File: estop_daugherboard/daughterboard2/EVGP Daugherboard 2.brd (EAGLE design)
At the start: 82.6 x 94.6 mm, 39 parts, among them J1 E-STOP HEADER, J2 AVR_SPI_PROG_3X2PTH, J3 UX60-MB-5S8, U1 ATMEGA32U4-AU, U4 NL27WZ08USG, U5 N_FET1, U6 N_FET2, X1 TSX-3225 16.0000MF18X-AC0, X2 JST-XH-02-PIN-LONG-PAD, X3 JST-XH-02-PIN-LONG-PAD, X5 JST-XH-03-PIN-LONG-PAD, X6 JST-XH-03-PIN-LONG-PAD

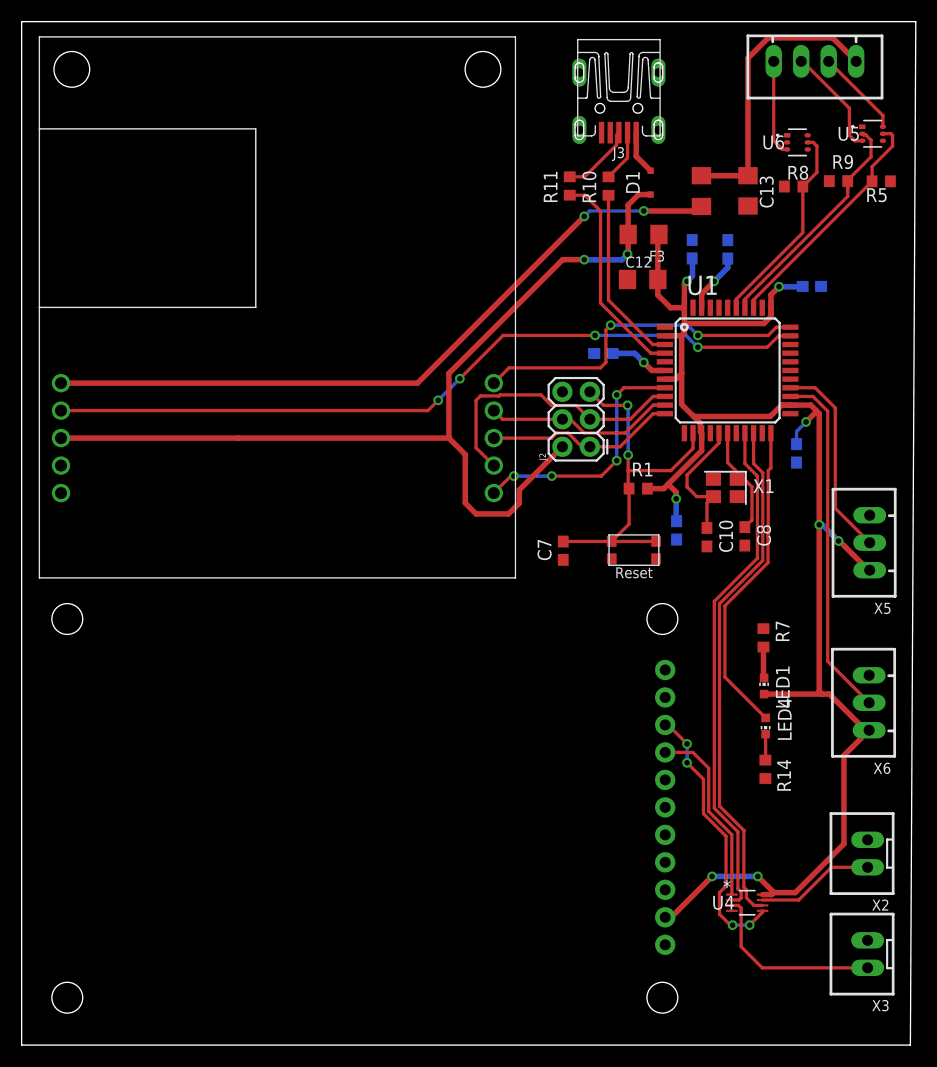
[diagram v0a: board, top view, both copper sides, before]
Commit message: Fixed up silkscreen
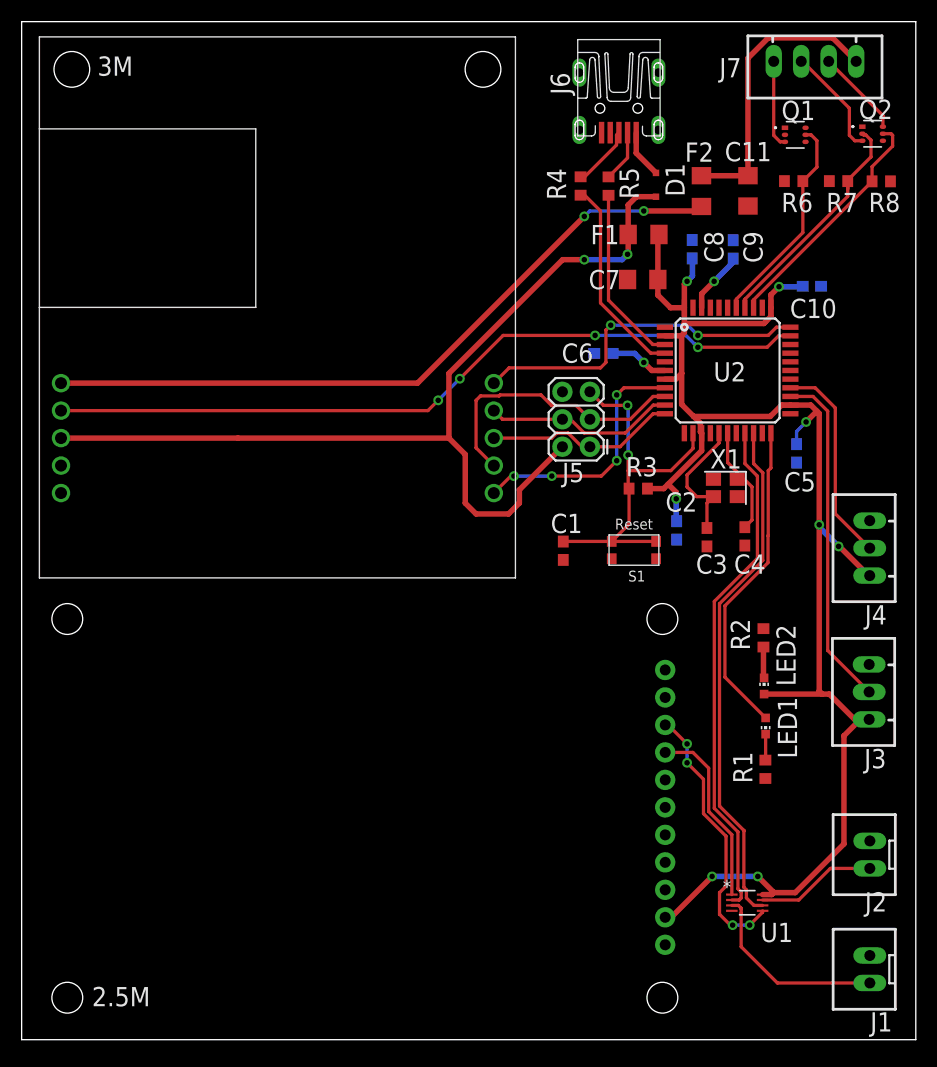
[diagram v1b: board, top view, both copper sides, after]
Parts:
- removed C12: 47uF, rcl:C1206
- removed LED4: BLUE, led:CHIP-LED0603
- removed R10, R11: 22 Ω, rcl:R0603
- removed R14: 330Ω, rcl:R0603
- removed R9: 10kΩ, rcl:R0603
- removed U4: NL27WZ08USG, DownloadedFiles:US8_2P40X2P10
- removed U6: N_FET2, DownloadedParts:SOT-363
- removed X2, X3: JST-XH-02-PIN-LONG-PAD, Rembrandt Electronics - JST XH Connectors v1-0:JST-XH-02-PACKAGE-LONG-PAD
- removed X5, X6: JST-XH-03-PIN-LONG-PAD, Rembrandt Electronics - JST XH Connectors v1-0:JST-XH-03-PACKAGE-LONG-PAD
- added C9: 10 nF, resistor:C0603
- added J4: JST-XH-03-PIN-LONG-PAD, Rembrandt Electronics - JST XH Connectors v1-0:JST-XH-03-PACKAGE-LONG-PAD
- added J5: AVR_SPI_PROG_3X2PTH, SparkFun-Connectors:2X3
- added J6: UX60-MB-5S8, RoboJackets-Connectors:UX60-MB-5S8
- added LED2: GREEN, led:CHIP-LED0603
- added Q1: N_FET2, DownloadedParts:SOT-363
- added R2: 330Ω, rcl:R0603
- added R3: 10k, rcl:R0603
- added R4: 22 Ω, rcl:R0603
- added R6: 10kΩ, rcl:R0603
- added RADIO: E-STOP HEADER, board_outline:RADIO_V1.3
- added U$1: (no value), RoboJackets-Aesthetics:ROBOBUZZ_1.0X
- added U2: ATMEGA32U4-AU, estop-v1.0:TQFP44
- C1: value 0.1 uF -> 0.1uF; device resistor:C0603 -> rcl:C0603
- C10, C8: value 9pF -> 0.1 uF
- C3: value 0.1 uF -> 9pF
- C4: value 1 uF -> 9pF
- C6: value 10 nF -> 1 uF
- C7: value 0.1uF -> 47uF; device rcl:C0603 -> rcl:C1206
- J1: value E-STOP HEADER -> JST-XH-02-PIN-LONG-PAD; device board_outline:RADIO_V1.3 -> Rembrandt Electronics - JST XH Connectors v1-0:JST-XH-02-PACKAGE-LONG-PAD
- J2: value AVR_SPI_PROG_3X2PTH -> JST-XH-02-PIN-LONG-PAD; device SparkFun-Connectors:2X3 -> Rembrandt Electronics - JST XH Connectors v1-0:JST-XH-02-PACKAGE-LONG-PAD
- J3: value UX60-MB-5S8 -> JST-XH-03-PIN-LONG-PAD; device RoboJackets-Connectors:UX60-MB-5S8 -> Rembrandt Electronics - JST XH Connectors v1-0:JST-XH-03-PACKAGE-LONG-PAD
- LED1: value GREEN -> BLUE
- R1: value 10k -> 330Ω
- R5: value 10kΩ -> 22 Ω
- R7: value 330Ω -> 10kΩ
- U1: value ATMEGA32U4-AU -> NL27WZ08USG; device estop-v1.0:TQFP44 -> DownloadedFiles:US8_2P40X2P10
- moved J1 84.2 mm to (84.4, 0.92), flipped to the top, turned to 90 degrees
- moved J3 64.6 mm to (84.3, 26.6), turned to 90 degrees
- moved U1 49.2 mm to (73.1, 7.07)
- moved J2 45.7 mm to (84.4, 11.5)
- moved R7 42.8 mm to (81.5, 73.8), turned to 0 degrees
- moved C1 30.3 mm to (56.1, 39.6), flipped to the top, turned to 270 degrees
- moved R1 28.5 mm to (74.7, 19.4), turned to 90 degrees
- moved C8 27.0 mm to (68.0, 67.5), flipped to the bottom, turned to 90 degrees
- moved C7 26.1 mm to (63.4, 64.7), turned to 0 degrees
- moved C2 25.8 mm to (66.5, 41.5), turned to 270 degrees
- moved R5 25.2 mm to (60.2, 73.3), turned to 90 degrees
- moved C10 25.1 mm to (79.0, 64.0), flipped to the bottom, turned to 180 degrees
- moved C4 21.4 mm to (72.8, 40.9), flipped to the top, turned to 270 degrees
- moved C6 15.0 mm to (59.8, 57.8), turned to 0 degrees
- moved R8 8.11 mm to (85.5, 73.7), turned to 180 degrees
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- renumbered C13 to C11, F3 to F1, F4 to F2, JST to J7, U5 to Q2
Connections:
- net 5V: now also C10.1, C7.2, C8.1, J3.1, J4.1, LED2.A, R3.2, RADIO.10, U1.8, U2.14, U2.2, U2.24, U2.34, U2.44, U2.7; no longer C1.1, C12.2, C3.1, J1.10, LED1.A, R1.2, U1.14, U1.2, U1.24, U1.34, U1.44, U1.7, U4.8, X5.1, X6.1
- net 5V_UNFUSED: now also J5.2; no longer J2.2
- net AREF: now also C9.1, U2.42; no longer C6.1, U1.42
- net DATA_N: now also R5.1, U2.3; no longer R10.1, U1.3
- net DATA_P: now also R4.1, U2.4; no longer R11.1, U1.4
- net DRIVE_EN: now also J2.1, U1.7; no longer U4.7, X2.1
- net DRIVE_EN_DB: now also U1.6, U2.20; no longer U1.20, U4.6
- net DRIVE_EN_RB: now also RADIO.3, U1.5; no longer J1.3, U4.5
- net ETH_RST: now also U2.32; no longer U1.32
- net GND: now also C7.1, C9.2, J1.2, J2.2, J3.3, J4.3, J5.6, J6.5, Q1.4, R1.1, R2.1, R6.1, RADIO.1, RADIO.11, U1.4, U2.15, U2.23, U2.35, U2.43, U2.5; no longer C12.1, C7.2, J1.1, J1.11, J2.6, J3.5, R14.1, R5.1, R9.1, U1.15, U1.23, U1.35, U1.43, U1.5, U4.4, U6.4, X2.2, X3.2, X5.3, X6.3
- net INTERRUPT: now also U2.33; no longer U1.33
- net LED1: now also LED1.A, U2.22; no longer LED4.A, U1.22
- net MCU_RST: now also C1.1, J5.5, R3.1, U2.13; no longer C7.1, J2.5, R1.1, U1.13
- net MISO: now also J5.1, U2.11; no longer J2.1, U1.11
- net MOSI: now also J5.4, U2.10; no longer J2.4, U1.10
- net N$11: now also J6.3, R4.2; no longer J3.3, R11.2
- net N$3: now also LED2.C, R2.2; no longer LED1.C, R7.2
- net N$5: now also J6.2, R5.2; no longer J3.2, R10.2
- net N$6: now also LED1.C, R1.2; no longer LED4.C, R14.2
- net N$7: now also J6.1; no longer J3.1
- net SCK: now also J5.3, U2.9; no longer J2.3, U1.9
- net SENSOR1: now also J4.2, U2.26; no longer U1.26, X5.2
- net SENSOR2: now also J3.2, U2.25; no longer U1.25, X6.2
- net SS: now also U2.8; no longer U1.8
- net STACK_CON3: now also Q1.3; no longer U6.3
- net STACK_MCU1: now also R8.2, U2.36; no longer R5.2, U1.36
- net STACK_MCU2: now also R7.2, U2.37; no longer R9.2, U1.37
- net STACK_MCU3: now also Q1.5, R6.2, U2.38; no longer R8.2, U1.38, U6.5
- net STEERING_EN: now also J1.1, U1.3; no longer U4.3, X3.1
- net STEERING_EN_DB: now also U1.2, U2.19; no longer U1.19, U4.2
- net STEERING_EN_RB: now also RADIO.4, U1.1; no longer J1.4, U4.1
- net UCAP: now also C6.1, U2.6; no longer C4.1, U1.6
- net XTAL1: now also C4.1, U2.17; no longer C8.1, U1.17
- net XTAL2: now also C3.1, U2.16; no longer C10.1, U1.16
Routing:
- net SENSOR2: track 32.5 -> 31.5 mm
- net N$11: track 6.77 -> 5.77 mm
- net DATA_P: track 19.8 -> 18.8 mm
- net STACK_MCU3: track 19.0 -> 19.8 mm
- net STACK_CON3: track 8.91 -> 8.13 mm
- net STEERING_EN: track 17.0 -> 17.8 mm
- net 5V: track 147.4 -> 148.1 mm
- net SENSOR1: track 18.7 -> 19.2 mm
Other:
- board size 82.6 x 94.6 mm -> 82.6 x 94.1 mm
- board text added: "2.5M"
- board text added: "3M"

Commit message: GND Plane and GND Vias, silkscreen updates
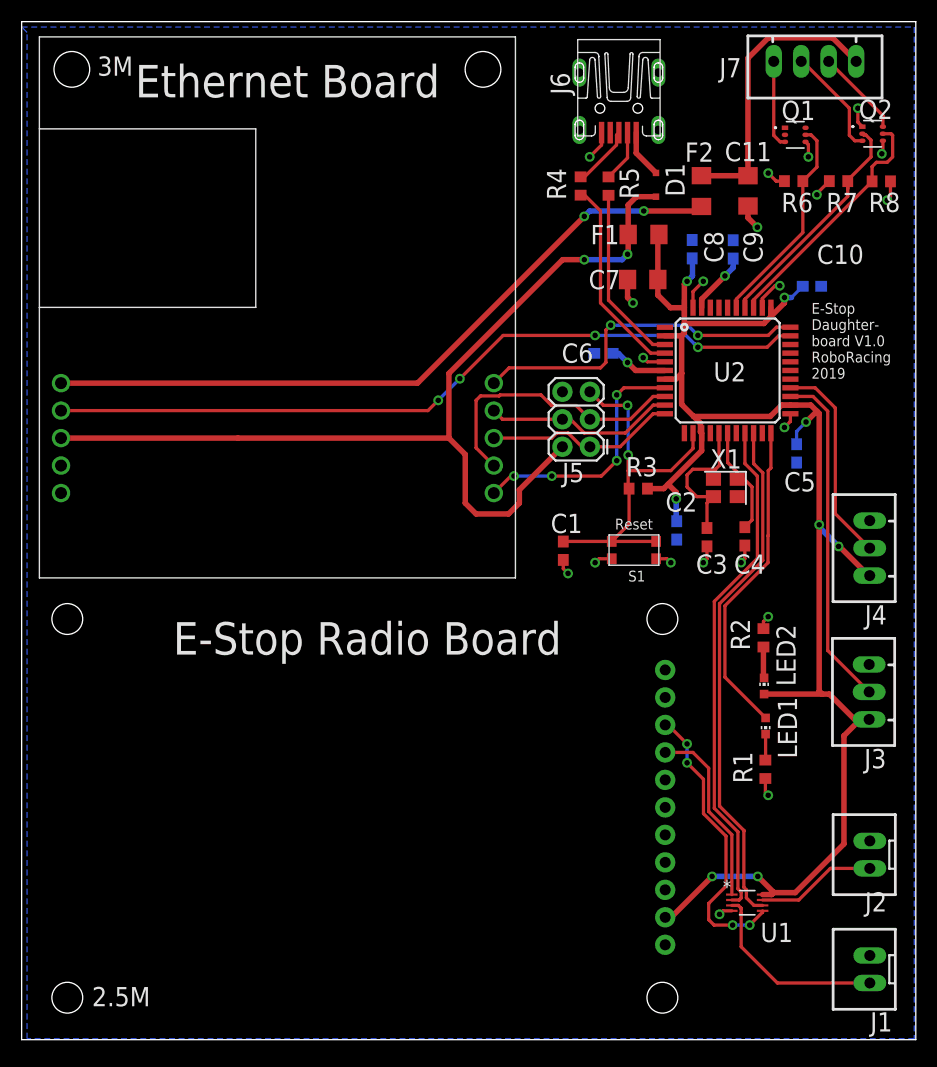
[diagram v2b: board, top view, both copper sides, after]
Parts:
- added U$3: (no value), RoboJackets-Aesthetics:ROBOJACKETS
- moved U$1 44.8 mm to (19.5, 8.00)
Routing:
- net GND: track 0.00 -> 39.1 mm, vias 0 -> 21
- net DRIVE_EN_RB: track 25.2 -> 27.0 mm
- net XTAL2: track 12.1 -> 13.4 mm
- net STACK_MCU1: track 22.2 -> 22.8 mm
- added copper zone on layer 16, net GND
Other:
- board text added: "E-Stop Daughter- board V1.0 RoboRacing 2019"
- board text added: "E-Stop Radio Board"
- board text added: "Ethernet Board"

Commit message: silkscreen updates, names
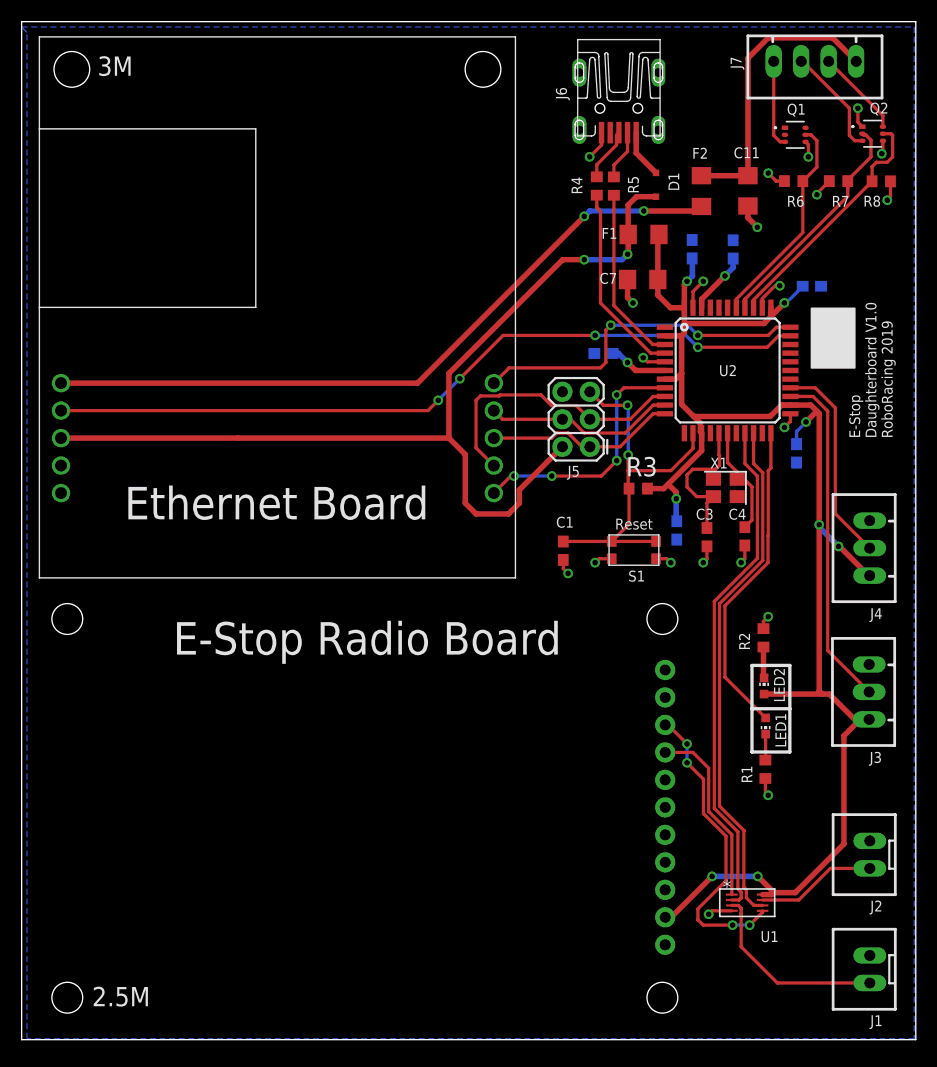
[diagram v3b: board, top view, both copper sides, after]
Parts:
- moved U$1 13.8 mm to (28.5, -2.50)
- moved U$3 13.3 mm to (59.0, -3.00)
- moved R4 1.50 mm to (59.2, 73.3)
- moved R5 0.50 mm to (60.7, 73.3)
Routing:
- net DRIVE_EN_RB: track 27.0 -> 28.4 mm
- net GND: track 39.1 -> 40.1 mm
- net DATA_P: track 18.8 -> 18.0 mm
- net N$11: track 5.77 -> 4.92 mm
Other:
- board text added: "E-Stop Daughterboard V1.0 RoboRacing 2019"
- board text removed: "E-Stop Daughter- board V1.0 RoboRacing 2019"

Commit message: Added the library
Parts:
- moved RADIO 39.5 mm to (7.72, -3.71), flipped to the top, turned to 0 degrees
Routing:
- net 5V: track 147.7 -> 168.0 mm, vias 8 -> 9
- net DRIVE_EN_RB: track 28.4 -> 43.2 mm, vias 4 -> 5
- net STEERING_EN_RB: track 17.2 -> 26.8 mm, vias 0 -> 1
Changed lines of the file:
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@@
 <?xml version="1.0" encoding="utf-8"?>
 <!DOCTYPE eagle SYSTEM "eagle.dtd">
-<eagle version="9.5.0">
+<eagle version="9.5.1">
 <drawing>
 <settings>
@@
 <attribute name="NAME" x="67.96" y="75.83" size="1" layer="25" font="vector"/>
 </element>
-<element name="RADIO" library="board_outline" package="RADIO_V1.3" value="E-STOP HEADER" x="7.72" y="35.79" smashed="yes" rot="MR180"/>
+<element name="RADIO" library="board_outline" package="RADIO_V1.3" value="E-STOP HEADER" x="7.72" y="-3.71" smashed="yes"/>
 <element name="J5" library="SparkFun-Connectors" library_urn="urn:adsk.eagle:library:513" package="2X3" package3d_urn="urn:adsk.eagle:package:38016/1" value="AVR_SPI_PROG_3X2PTH" x="58.52" y="49.21" smashed="yes" rot="R90">
 <attribute name="NAME" x="56.456" y="46.44" size="1" layer="25" font="vector"/>
@@
 <via x="69.8126" y="9.5" extent="1-16" drill="0.508"/>
 <wire x1="69.8126" y1="9.5" x2="66.0326" y2="5.72" width="0.508" layer="1"/>
-<wire x1="66.0326" y1="5.72" x2="65.48" y2="5.72" width="0.508" layer="1"/>
+<wire x1="66.0326" y1="5.72" x2="65.6662875" y2="6.0863125" width="0.508" layer="16"/>
+<wire x1="65.6662875" y1="6.0863125" x2="65.48" y2="26.36" width="0.508" layer="16"/>
 <wire x1="74.62" y1="26.35" x2="80" y2="26.35" width="0.508" layer="1"/>
 <wire x1="80" y1="26.35" x2="80.65" y2="26.35" width="0.508" layer="1"/>
@@
 <wire x1="76.5" y1="62.5" x2="76.5" y2="62.49934375" width="0.508" layer="1"/>
 <wire x1="76.5" y1="62.49934375" x2="75.25" y2="61.24934375" width="0.508" layer="1"/>
+<via x="66.0326" y="5.72" extent="1-16" drill="0.35"/>
 </signal>
 <signal name="MCU_RST">
@@
 <contactref element="U1" pad="5"/>
 <contactref element="RADIO" pad="3"/>
-<wire x1="65.48" y1="23.5" x2="65.7474" y2="23.5" width="0.3048" layer="1"/>
+<wire x1="65.48" y1="8.58" x2="65.3223125" y2="23.0749125" width="0.3048" layer="16"/>
+<wire x1="65.3223125" y1="23.0749125" x2="65.7474" y2="23.5" width="0.3048" layer="16"/>
 <wire x1="65.7474" y1="23.5" x2="67.5" y2="21.7474" width="0.3048" layer="1"/>
 <via x="67.5" y="21.7474" extent="1-16" drill="0.508"/>
@@
 <wire x1="69" y1="5" x2="71.7126" y2="5" width="0.3048" layer="1"/>
 <wire x1="68.5" y1="5.5" x2="68.5" y2="6.5" width="0.3048" layer="1"/>
+<via x="65.7474" y="23.5" extent="1-16" drill="0.35"/>
 </signal>
 <signal name="STEERING_EN_RB">
@@
 <contactref element="RADIO" pad="4"/>
 <wire x1="71.6376" y1="7.82" x2="71.6376" y2="13.3624" width="0.3048" layer="1"/>
-<wire x1="68.04" y1="20.96" x2="65.48" y2="20.96" width="0.3048" layer="1"/>
+<wire x1="68.04" y1="20.96" x2="68.04" y2="11.34095625" width="0.3048" layer="16"/>
+<wire x1="68.04" y1="11.34095625" x2="65.48" y2="11.12" width="0.3048" layer="16"/>
 <wire x1="71.6376" y1="13.3624" x2="69.5" y2="15.5" width="0.3048" layer="1"/>
 <wire x1="69.5" y1="19.5" x2="68.04" y2="20.96" width="0.3048" layer="1"/>
 <wire x1="69.5" y1="15.5" x2="69.5" y2="19.5" width="0.3048" layer="1"/>
+<via x="68.04" y="20.96" extent="1-16" drill="0.35"/>
 </signal>
 <signal name="DRIVE_EN_DB">
@@
 <wire x1="58.5" y1="71" x2="58" y2="70.5" width="0.508" layer="16"/>
 <via x="58" y="70.5" extent="1-16" drill="0.508"/>
-<wire x1="58" y1="70.5" x2="42.59" y2="55.09" width="0.508" layer="1"/>
-<wire x1="42.59" y1="55.09" x2="9.64" y2="55.09" width="0.508" layer="1"/>
+<wire x1="58" y1="70.5" x2="42.59" y2="55.09" width="0.2" layer="1"/>
+<wire x1="42.59" y1="55.09" x2="9.64" y2="55.09" width="0.2" layer="1"/>
 </signal>
 </signals>
